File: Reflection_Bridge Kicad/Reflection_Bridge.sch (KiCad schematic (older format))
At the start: 7 parts, among them P1 SMA_Female, P2 SMA_Female, P3 SMA_Female, T1 Transformer_1P_1S

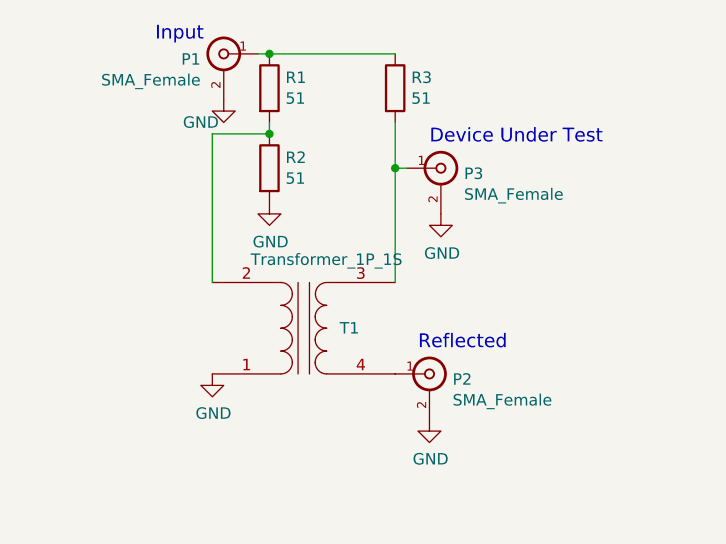
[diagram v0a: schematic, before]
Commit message: Added notes to fix T1 footprint on the reflection bridge.
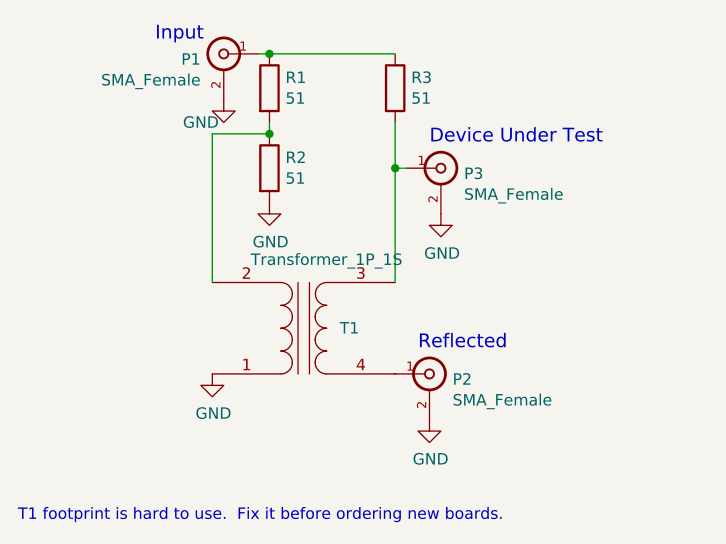
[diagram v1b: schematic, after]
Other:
- note added: "T1 footprint is hard to use. Fix it before ordering new boards."
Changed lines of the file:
@@
 EESchema Schematic File Version 4
 LIBS:Reflection_Bridge-cache
-EELAYER 26 0
+EELAYER 29 0
 EELAYER END
 $Descr USLetter 11000 8500
@@
 Wire Wire Line
 	5150 3850 5150 4350
+Text Notes 3500 5400 0    50   ~ 0
+T1 footprint is hard to use.  Fix it before ordering new boards.
 $EndSCHEMATC

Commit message: Added v0.2 of reflection bridge.
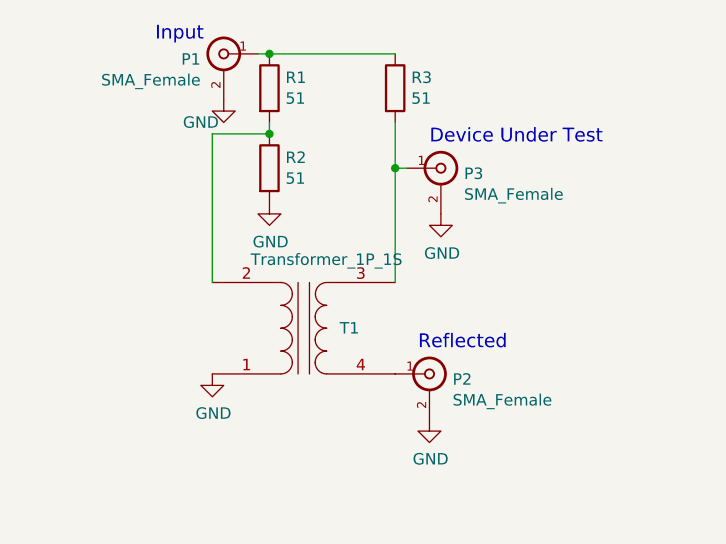
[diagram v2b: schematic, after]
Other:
- note removed: "T1 footprint is hard to use. Fix it before ordering new boards."
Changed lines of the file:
@@
 Sheet 1 1
 Title "Reflection Bridge"
-Date "2017-04-20"
-Rev "0.1"
+Date "2019-05-16"
+Rev "0.2"
 Comp "Walla Walla University"
 Comment1 "Rob Frohne"
@@
 Wire Wire Line
 	5150 3850 5150 4350
-Text Notes 3500 5400 0    50   ~ 0
-T1 footprint is hard to use.  Fix it before ordering new boards.
 $EndSCHEMATC
